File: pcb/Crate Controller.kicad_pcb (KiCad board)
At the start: 2 copper layers, 111.4 x 30.1 mm, 10 parts, among them J1 1984691, U2 LM317_TO-220

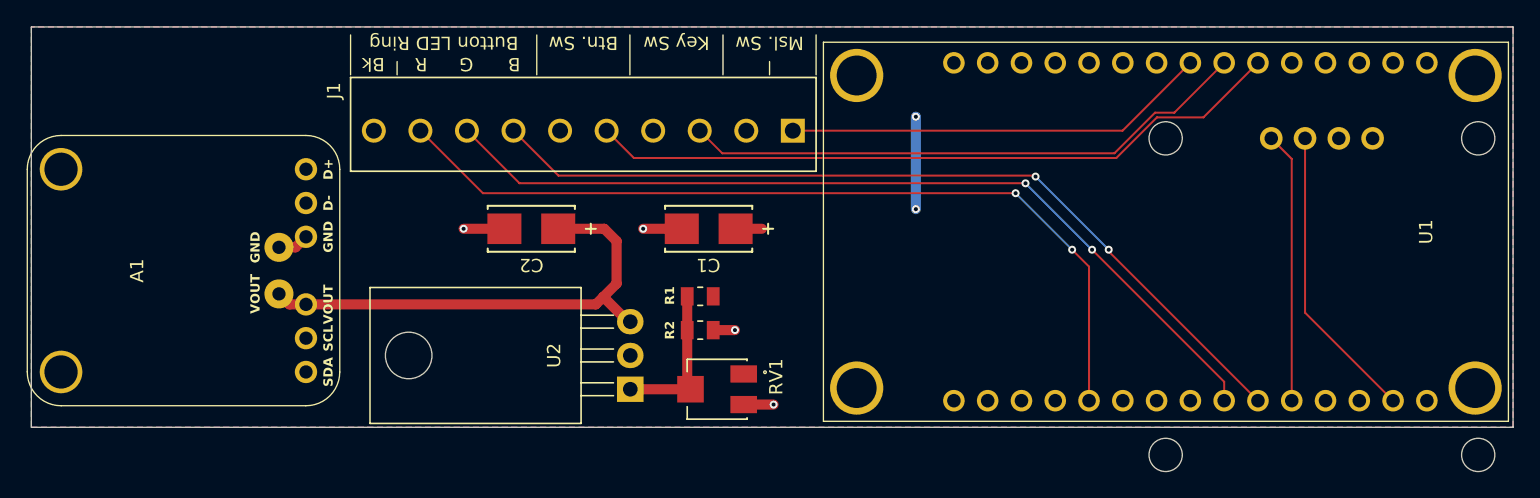
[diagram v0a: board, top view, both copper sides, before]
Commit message: Update PCB to v1
PCB sent to first prod trial
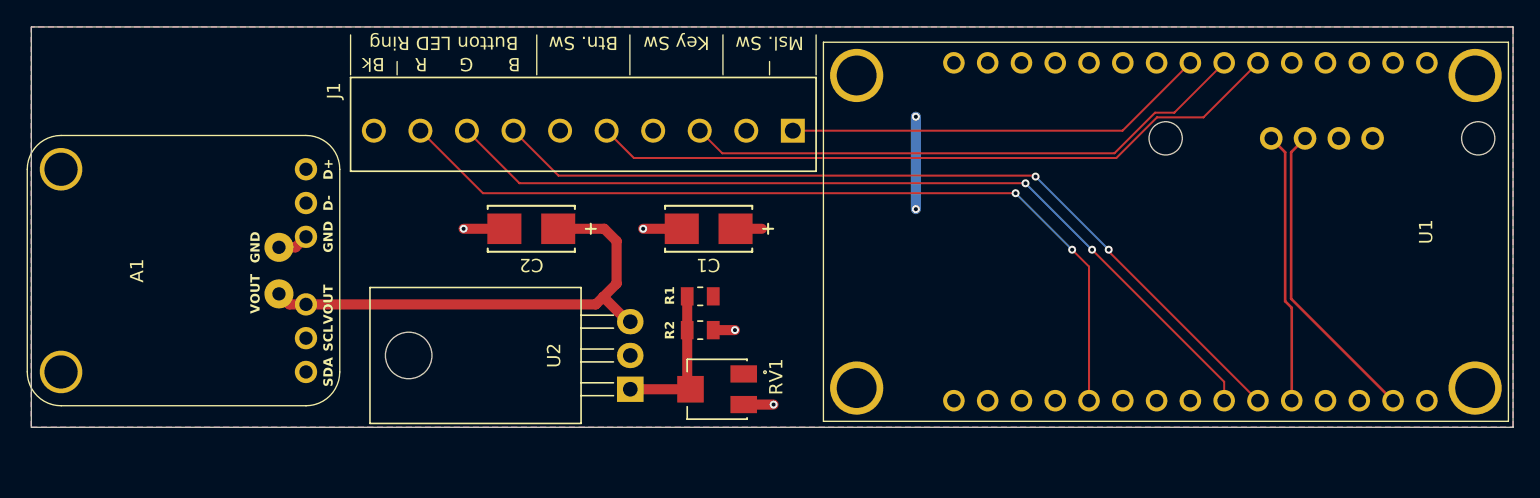
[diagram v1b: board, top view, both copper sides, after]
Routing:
- net /SCL: track 22.5 -> 23.3 mm
